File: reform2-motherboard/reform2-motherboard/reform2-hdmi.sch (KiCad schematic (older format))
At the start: 12 parts

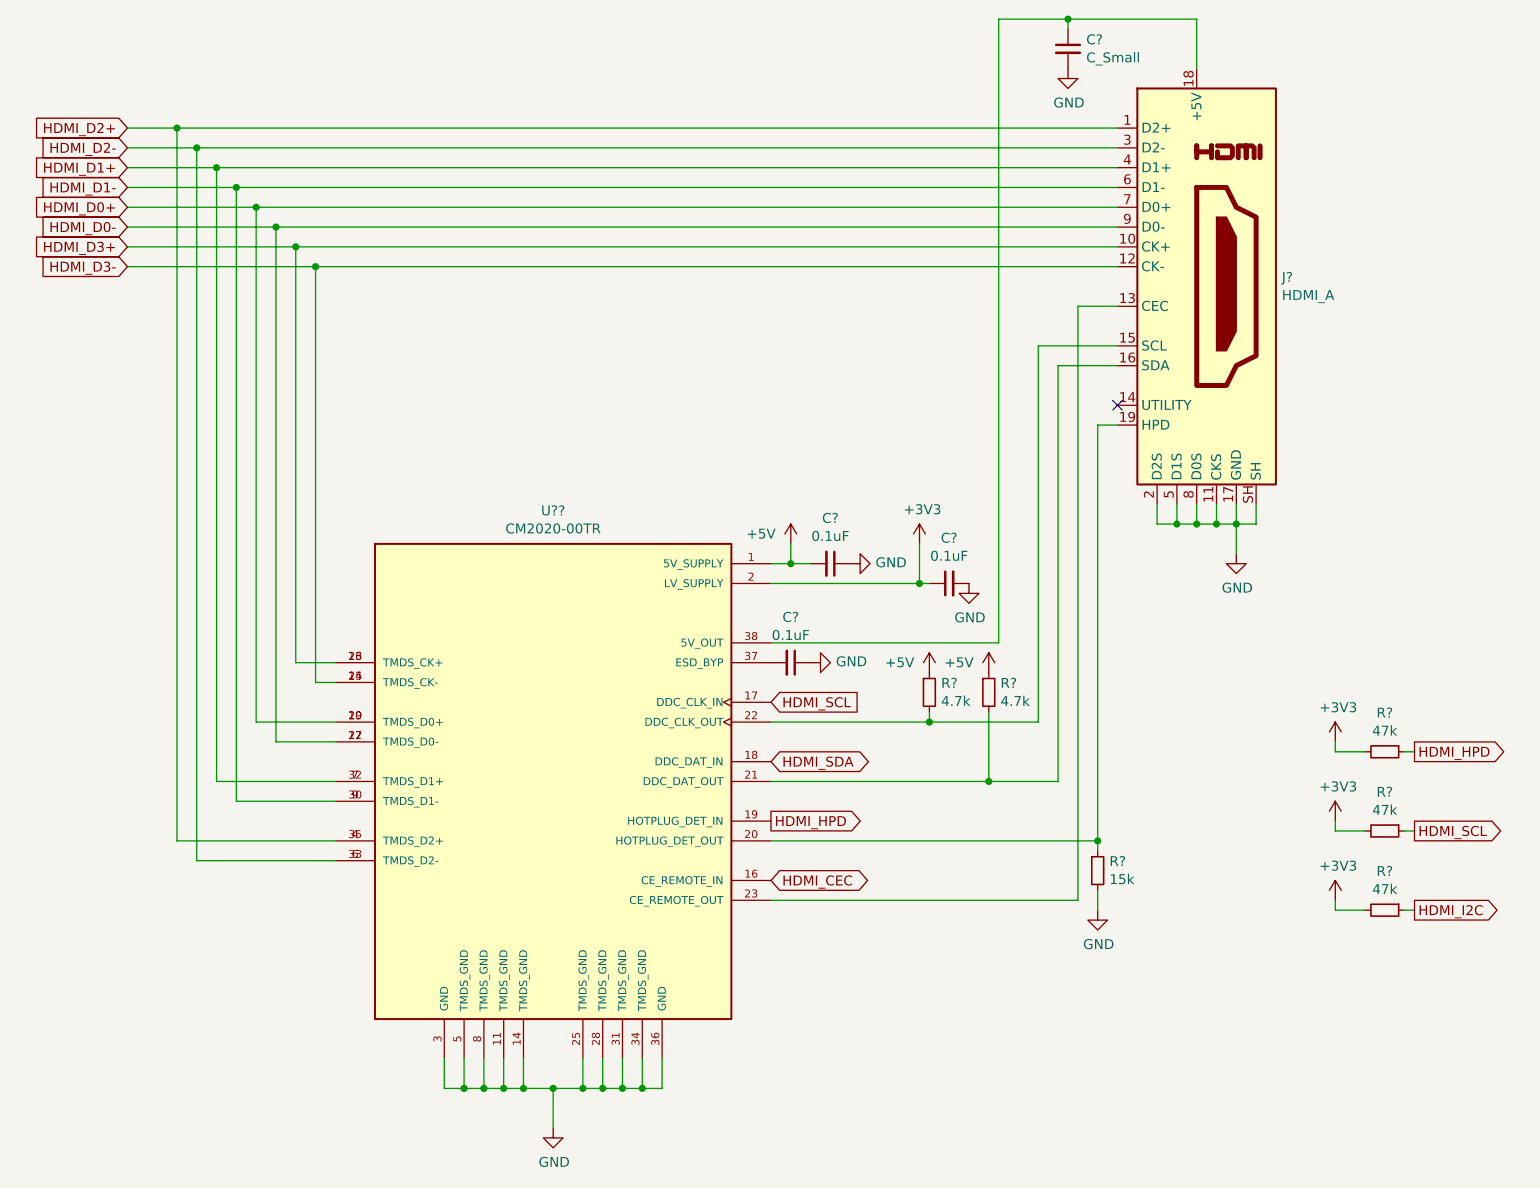
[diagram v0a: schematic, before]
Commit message: reform2: schematic work, mainly power, display, first footprint tests
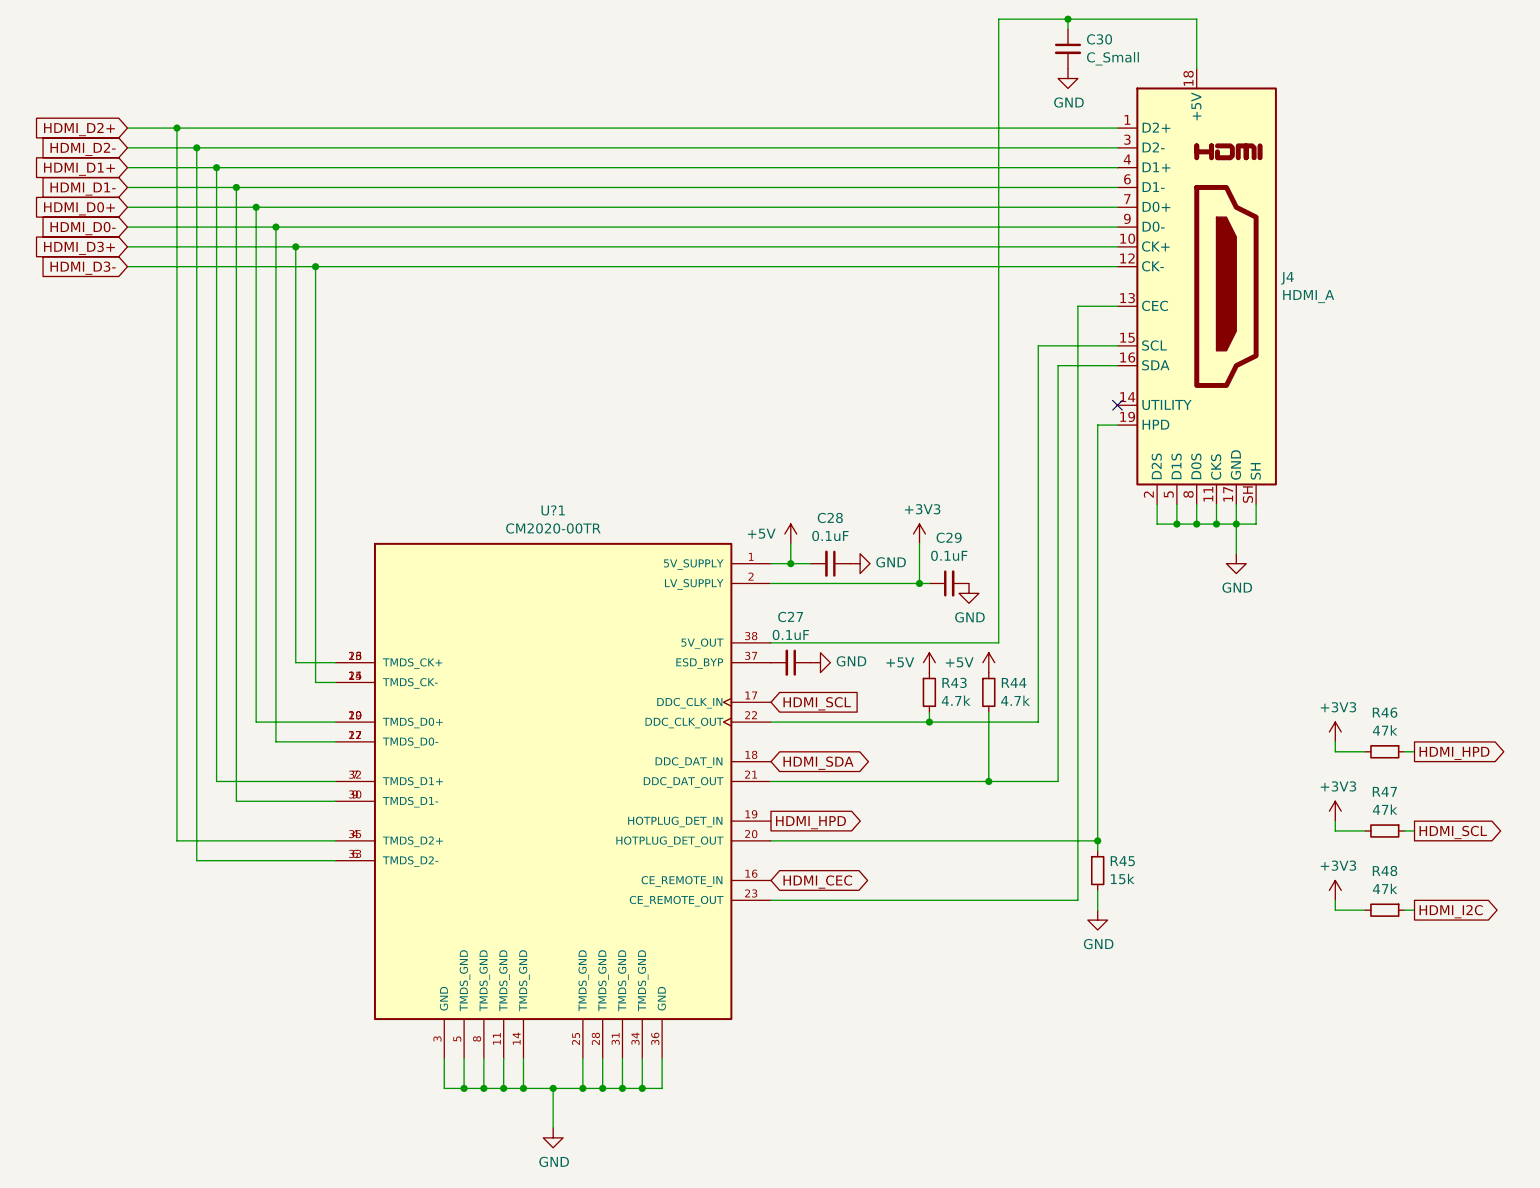
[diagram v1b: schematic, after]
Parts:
- C27, C28, C29, C30: renamed from C?; footprint (none) -> Capacitor_SMD:C_0603_1608Metric
- J4: renamed from J?; footprint (none) -> Connector_HDMI:HDMI_A_Contact_Technology_HDMI-19APL2_Horizontal
- R43, R44, R45, R46, R47, R48: renamed from R?; footprint (none) -> Resistor_SMD:R_0603_1608Metric
- U?1: renamed from U??; footprint TSSOP50P640X120-38N -> footprints:TSSOP50P640X120-38N
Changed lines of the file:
@@
 P 8050 2600
 AR Path="/5D123420" Ref="J?"  Part="1"
-AR Path="/5D0D8363/5D123420" Ref="J?"  Part="1"
-F 0 "J?" H 8480 2646 50  0000 L CNN
+AR Path="/5D0D8363/5D123420" Ref="J4"  Part="1"
+F 0 "J4" H 8480 2646 50  0000 L CNN
 F 1 "HDMI_A" H 8480 2555 50  0000 L CNN
-F 2 "" H 8075 2600 50  0001 C CNN
+F 2 "Connector_HDMI:HDMI_A_Contact_Technology_HDMI-19APL2_Horizontal" H 8075 2600 50  0001 C CNN
 F 3 "https://en.wikipedia.org/wiki/HDMI" H 8075 2600 50  0001 C CNN
 	1    8050 2600
@@
 HDMI_D0+
 $Comp
-L reform2:CM2020-00TR U??
+L reform2:CM2020-00TR U?1
 U 1 1 5D124B0E
 P 4800 5100
-F 0 "U??" H 4800 6467 50  0000 C CNN
+F 0 "U?1" H 4800 6467 50  0000 C CNN
 F 1 "CM2020-00TR" H 4800 6376 50  0000 C CNN
-F 2 "TSSOP50P640X120-38N" H 4350 2950 50  0001 L BNN
+F 2 "footprints:TSSOP50P640X120-38N" H 4350 2950 50  0001 L BNN
 F 3 "" H 4800 5100 50  0001 L BNN
 F 4 "CM2020-00TR Series 10.8 V HDMI Transmitter Port Protection and Interface Device" H 3350 3150 50  0001 L BNN "Field6"
@@
 	2900 1800 7650 1800
 $Comp
-L power:GND #PWR?
+L power:GND #PWR0156
 U 1 1 5D12D351
 P 4800 6850
-F 0 "#PWR?" H 4800 6600 50  0001 C CNN
+F 0 "#PWR0156" H 4800 6600 50  0001 C CNN
 F 1 "GND" H 4805 6677 50  0000 C CNN
 F 2 "" H 4800 6850 50  0001 C CNN
@@
 	7250 2900 7650 2900
 $Comp
-L power:GND #PWR?
+L power:GND #PWR0157
 U 1 1 5D137F78
 P 8250 3950
-F 0 "#PWR?" H 8250 3700 50  0001 C CNN
+F 0 "#PWR0157" H 8250 3700 50  0001 C CNN
 F 1 "GND" H 8255 3777 50  0000 C CNN
 F 2 "" H 8250 3950 50  0001 C CNN
@@
 	8250 3800 8250 3950
 $Comp
-L Device:R_Small R?
+L Device:R_Small R45
 U 1 1 5D13F480
 P 7550 5550
-F 0 "R?" H 7609 5596 50  0000 L CNN
+F 0 "R45" H 7609 5596 50  0000 L CNN
 F 1 "15k" H 7609 5505 50  0000 L CNN
-F 2 "" H 7550 5550 50  0001 C CNN
+F 2 "Resistor_SMD:R_0603_1608Metric" H 7550 5550 50  0001 C CNN
 F 3 "~" H 7550 5550 50  0001 C CNN
 	1    7550 5550
@@
 Connection ~ 7550 5400
 $Comp
-L power:GND #PWR?
+L power:GND #PWR0158
 U 1 1 5D14251A
 P 7550 5750
-F 0 "#PWR?" H 7550 5500 50  0001 C CNN
+F 0 "#PWR0158" H 7550 5500 50  0001 C CNN
 F 1 "GND" H 7555 5577 50  0000 C CNN
 F 2 "" H 7550 5750 50  0001 C CNN
@@
 	8050 1250 8050 1500
 $Comp
-L Device:C_Small C?
+L Device:C_Small C30
 U 1 1 5D14719E
 P 7400 1400
-F 0 "C?" H 7492 1446 50  0000 L CNN
+F 0 "C30" H 7492 1446 50  0000 L CNN
 F 1 "C_Small" H 7492 1355 50  0000 L CNN
-F 2 "" H 7400 1400 50  0001 C CNN
+F 2 "Capacitor_SMD:C_0603_1608Metric" H 7400 1400 50  0001 C CNN
 F 3 "~" H 7400 1400 50  0001 C CNN
 	1    7400 1400
@@
 	7400 1250 8050 1250
 $Comp
-L power:GND #PWR?
+L power:GND #PWR0159
 U 1 1 5D148EE2
 P 7400 1500
-F 0 "#PWR?" H 7400 1250 50  0001 C CNN
+F 0 "#PWR0159" H 7400 1250 50  0001 C CNN
 F 1 "GND" H 7405 1327 50  0000 C CNN
 F 2 "" H 7400 1500 50  0001 C CNN
@@
 $EndComp
 $Comp
-L Device:R_Small R?
+L Device:R_Small R43
 U 1 1 5D14CD66
 P 6700 4650
-F 0 "R?" H 6759 4696 50  0000 L CNN
+F 0 "R43" H 6759 4696 50  0000 L CNN
 F 1 "4.7k" H 6759 4605 50  0000 L CNN
-F 2 "" H 6700 4650 50  0001 C CNN
+F 2 "Resistor_SMD:R_0603_1608Metric" H 6700 4650 50  0001 C CNN
 F 3 "~" H 6700 4650 50  0001 C CNN
 	1    6700 4650
@@
 	6700 4800 7250 4800
 $Comp
-L Device:R_Small R?
+L Device:R_Small R44
 U 1 1 5D14D233
 P 7000 4650
-F 0 "R?" H 7059 4696 50  0000 L CNN
+F 0 "R44" H 7059 4696 50  0000 L CNN
 F 1 "4.7k" H 7059 4605 50  0000 L CNN
-F 2 "" H 7000 4650 50  0001 C CNN
+F 2 "Resistor_SMD:R_0603_1608Metric" H 7000 4650 50  0001 C CNN
 F 3 "~" H 7000 4650 50  0001 C CNN
 	1    7000 4650
@@
 	7000 5100 7350 5100
 $Comp
-L power:+5V #PWR?
+L power:+5V #PWR0160
 U 1 1 5D1511E0
 P 6700 4550
-F 0 "#PWR?" H 6700 4400 50  0001 C CNN
+F 0 "#PWR0160" H 6700 4400 50  0001 C CNN
 F 1 "+5V" H 6550 4600 50  0000 C CNN
 F 2 "" H 6700 4550 50  0001 C CNN
@@
 $EndComp
 $Comp
-L power:+5V #PWR?
+L power:+5V #PWR0161
 U 1 1 5D1514E7
 P 7000 4550
-F 0 "#PWR?" H 7000 4400 50  0001 C CNN
+F 0 "#PWR0161" H 7000 4400 50  0001 C CNN
 F 1 "+5V" H 6850 4600 50  0000 C CNN
 F 2 "" H 7000 4550 50  0001 C CNN
@@
 $EndComp
 $Comp
-L power:+5V #PWR?
+L power:+5V #PWR0162
 U 1 1 5D151F10
 P 6000 3900
-F 0 "#PWR?" H 6000 3750 50  0001 C CNN
+F 0 "#PWR0162" H 6000 3750 50  0001 C CNN
 F 1 "+5V" H 5850 3950 50  0000 C CNN
 F 2 "" H 6000 3900 50  0001 C CNN
@@
 	6000 4000 5900 4000
 $Comp
-L power:+3V3 #PWR?
+L power:+3V3 #PWR0163
 U 1 1 5D1543CF
 P 6650 3900
-F 0 "#PWR?" H 6650 3750 50  0001 C CNN
+F 0 "#PWR0163" H 6650 3750 50  0001 C CNN
 F 1 "+3V3" H 6665 4073 50  0000 C CNN
 F 2 "" H 6650 3900 50  0001 C CNN
@@
 	6650 4100 5900 4100
 $Comp
-L Device:C_Small C?
+L Device:C_Small C29
 U 1 1 5D156EA0
 P 6800 4100
-F 0 "C?" V 7029 4100 50  0000 C CNN
+F 0 "C29" V 7029 4100 50  0000 C CNN
 F 1 "0.1uF" V 6938 4100 50  0000 C CNN
-F 2 "" H 6800 4100 50  0001 C CNN
+F 2 "Capacitor_SMD:C_0603_1608Metric" H 6800 4100 50  0001 C CNN
 F 3 "~" H 6800 4100 50  0001 C CNN
 	1    6800 4100
@@
 Connection ~ 6650 4100
 $Comp
-L power:GND #PWR?
+L power:GND #PWR0164
 U 1 1 5D15970D
 P 6900 4100
-F 0 "#PWR?" H 6900 3850 50  0001 C CNN
+F 0 "#PWR0164" H 6900 3850 50  0001 C CNN
 F 1 "GND" H 6905 3927 50  0000 C CNN
 F 2 "" H 6900 4100 50  0001 C CNN
@@
 $EndComp
 $Comp
-L Device:C_Small C?
+L Device:C_Small C28
 U 1 1 5D15C03F
 P 6200 4000
-F 0 "C?" V 5971 4000 50  0000 C CNN
+F 0 "C28" V 5971 4000 50  0000 C CNN
 F 1 "0.1uF" V 6062 4000 50  0000 C CNN
-F 2 "" H 6200 4000 50  0001 C CNN
+F 2 "Capacitor_SMD:C_0603_1608Metric" H 6200 4000 50  0001 C CNN
 F 3 "~" H 6200 4000 50  0001 C CNN
 	1    6200 4000
@@
 Connection ~ 6000 4000
 $Comp
-L power:GND #PWR?
+L power:GND #PWR0165
 U 1 1 5D1656C0
 P 6300 4000
-F 0 "#PWR?" H 6300 3750 50  0001 C CNN
+F 0 "#PWR0165" H 6300 3750 50  0001 C CNN
 F 1 "GND" V 6305 3872 50  0000 R CNN
 F 2 "" H 6300 4000 50  0001 C CNN
@@
 HDMI_HPD
 $Comp
-L power:+3V3 #PWR?
+L power:+3V3 #PWR0166
 U 1 1 5D16C7AF
 P 8750 4900
-F 0 "#PWR?" H 8750 4750 50  0001 C CNN
+F 0 "#PWR0166" H 8750 4750 50  0001 C CNN
 F 1 "+3V3" H 8765 5073 50  0000 C CNN
 F 2 "" H 8750 4900 50  0001 C CNN
@@
 $EndComp
 $Comp
-L Device:R_Small R?
+L Device:R_Small R46
 U 1 1 5D16CD31
 P 9000 4950
-F 0 "R?" V 8804 4950 50  0000 C CNN
+F 0 "R46" V 8804 4950 50  0000 C CNN
 F 1 "47k" V 8895 4950 50  0000 C CNN
-F 2 "" H 9000 4950 50  0001 C CNN
+F 2 "Resistor_SMD:R_0603_1608Metric" H 9000 4950 50  0001 C CNN
 F 3 "~" H 9000 4950 50  0001 C CNN
 	1    9000 4950
@@
 	8750 4950 8750 4900
 $Comp
-L Device:C_Small C?
+L Device:C_Small C27
 U 1 1 5D171FA3
 P 6000 4500
-F 0 "C?" V 5771 4500 50  0000 C CNN
+F 0 "C27" V 5771 4500 50  0000 C CNN
 F 1 "0.1uF" V 5862 4500 50  0000 C CNN
-F 2 "" H 6000 4500 50  0001 C CNN
+F 2 "Capacitor_SMD:C_0603_1608Metric" H 6000 4500 50  0001 C CNN
 F 3 "~" H 6000 4500 50  0001 C CNN
 	1    6000 4500
@@
 $EndComp
 $Comp
-L power:GND #PWR?
+L power:GND #PWR0167
 U 1 1 5D17234F
 P 6100 4500
-F 0 "#PWR?" H 6100 4250 50  0001 C CNN
+F 0 "#PWR0167" H 6100 4250 50  0001 C CNN
 F 1 "GND" V 6105 4372 50  0000 R CNN
 F 2 "" H 6100 4500 50  0001 C CNN
@@
 HDMI_SCL
 $Comp
-L power:+3V3 #PWR?
+L power:+3V3 #PWR0168
 U 1 1 5D1829AF
 P 8750 5300
-F 0 "#PWR?" H 8750 5150 50  0001 C CNN
+F 0 "#PWR0168" H 8750 5150 50  0001 C CNN
 F 1 "+3V3" H 8765 5473 50  0000 C CNN
 F 2 "" H 8750 5300 50  0001 C CNN
@@
 $EndComp
 $Comp
-L Device:R_Small R?
+L Device:R_Small R47
 U 1 1 5D1829B9
 P 9000 5350
-F 0 "R?" V 8804 5350 50  0000 C CNN
+F 0 "R47" V 8804 5350 50  0000 C CNN
 F 1 "47k" V 8895 5350 50  0000 C CNN
-F 2 "" H 9000 5350 50  0001 C CNN
+F 2 "Resistor_SMD:R_0603_1608Metric" H 9000 5350 50  0001 C CNN
 F 3 "~" H 9000 5350 50  0001 C CNN
 	1    9000 5350
@@
 HDMI_I2C
 $Comp
-L power:+3V3 #PWR?
+L power:+3V3 #PWR0169
 U 1 1 5D18542A
 P 8750 5700
-F 0 "#PWR?" H 8750 5550 50  0001 C CNN
+F 0 "#PWR0169" H 8750 5550 50  0001 C CNN
 F 1 "+3V3" H 8765 5873 50  0000 C CNN
 F 2 "" H 8750 5700 50  0001 C CNN
@@
 $EndComp
 $Comp
-L Device:R_Small R?
+L Device:R_Small R48
 U 1 1 5D185434
 P 9000 5750
-F 0 "R?" V 8804 5750 50  0000 C CNN
+F 0 "R48" V 8804 5750 50  0000 C CNN
 F 1 "47k" V 8895 5750 50  0000 C CNN
-F 2 "" H 9000 5750 50  0001 C CNN
+F 2 "Resistor_SMD:R_0603_1608Metric" H 9000 5750 50  0001 C CNN
 F 3 "~" H 9000 5750 50  0001 C CNN
 	1    9000 5750

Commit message: WIP: Reform2 more serious component placement on motherboard
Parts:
- J4: footprint Connector_HDMI:HDMI_A_Contact_Technology_HDMI-19APL2_Horizontal -> footprints:HDMI-685119134923
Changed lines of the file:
@@
 F 0 "J4" H 8480 2646 50  0000 L CNN
 F 1 "HDMI_A" H 8480 2555 50  0000 L CNN
-F 2 "Connector_HDMI:HDMI_A_Contact_Technology_HDMI-19APL2_Horizontal" H 8075 2600 50  0001 C CNN
+F 2 "footprints:HDMI-685119134923" H 8075 2600 50  0001 C CNN
 F 3 "https://en.wikipedia.org/wiki/HDMI" H 8075 2600 50  0001 C CNN
 	1    8050 2600

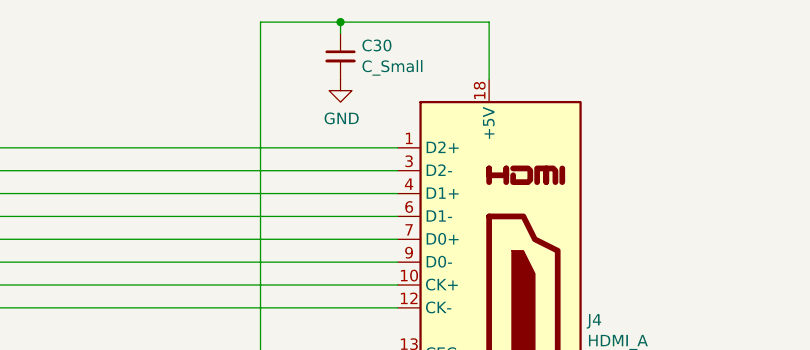
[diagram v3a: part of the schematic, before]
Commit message: WIP: reform2 motherboard: more sanity and footprint checks, passives
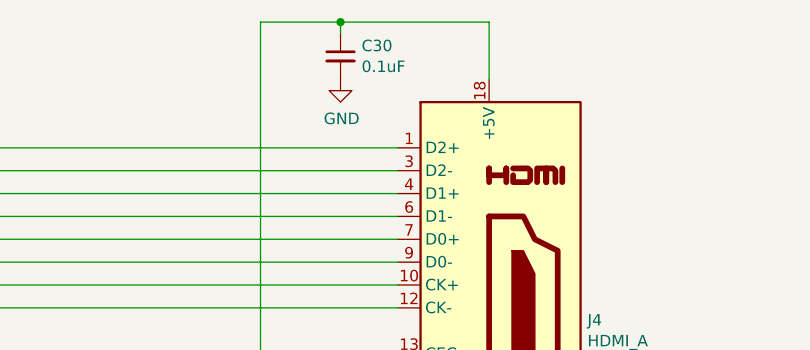
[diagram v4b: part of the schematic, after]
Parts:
- C30: value C_Small -> 0.1uF
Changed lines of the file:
@@
 Sheet 8 9
 Title "MNT Reform 2 External Display"
-Date "2019-06-21"
+Date "2019-07-03"
 Rev "0.1"
 Comp "MNT Research GmbH"
 Comment1 "https://mntre.com"
 Comment2 "Engineer: Lukas F. Hartmann"
-Comment3 ""
+Comment3 "License: GPL v3+"
 Comment4 ""
 $EndDescr
@@
 P 7400 1400
 F 0 "C30" H 7492 1446 50  0000 L CNN
-F 1 "C_Small" H 7492 1355 50  0000 L CNN
+F 1 "0.1uF" H 7492 1355 50  0000 L CNN
 F 2 "Capacitor_SMD:C_0603_1608Metric" H 7400 1400 50  0001 C CNN
 F 3 "~" H 7400 1400 50  0001 C CNN
